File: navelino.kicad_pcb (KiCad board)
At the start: 2 copper layers, 45.6 x 37.3 mm, 73 parts, among them CON1 USB, IC1 ATMEGA328P-A, M1 CONN_1, M2 CONN_1, P1 CONN_02X03, P3 CONN_6, SW0 SW_PUSH, SW1 SMD-SWITCH-TACTILE-SPST-NO(4P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, SW2 SMD-SWITCH-TACTILE-SPST-NO(4P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, U1 XC6204B332MR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

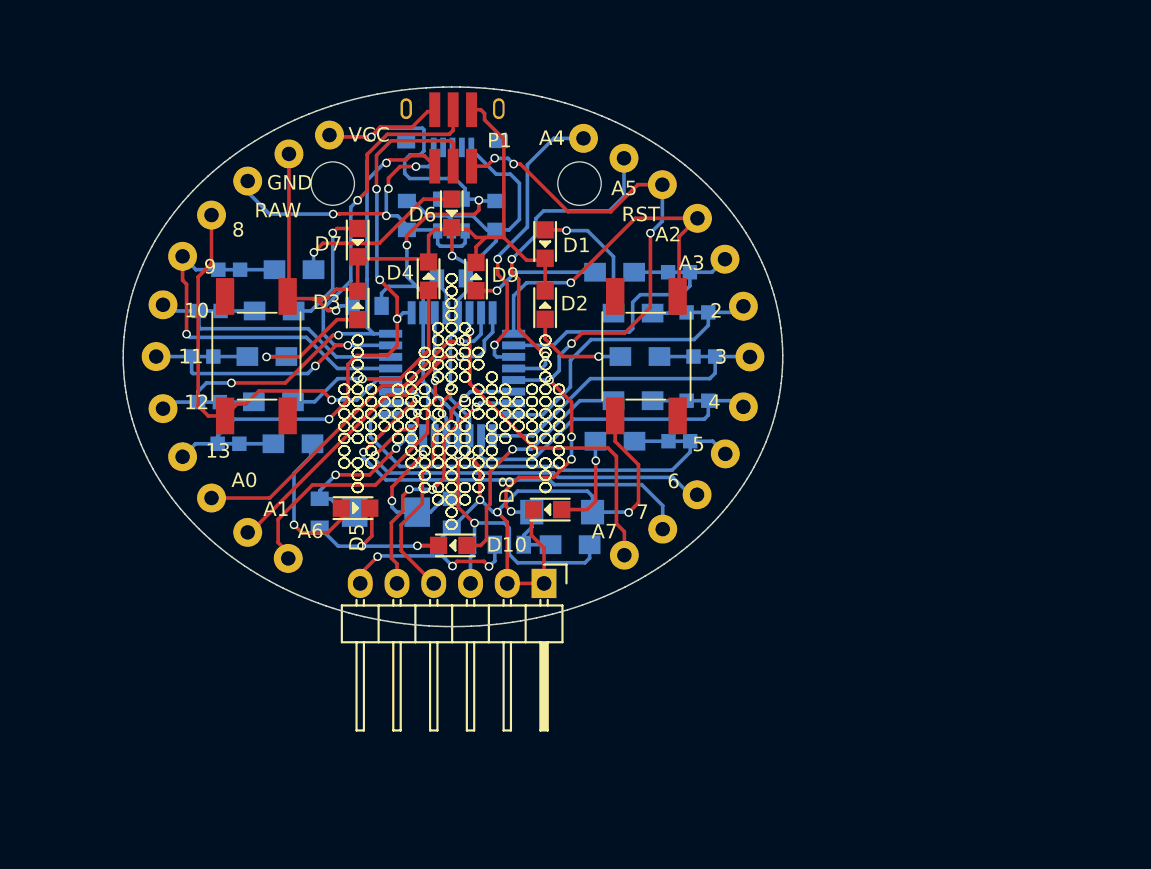
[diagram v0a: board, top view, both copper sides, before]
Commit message: Empezando rev3
- Permitir hojas intercambiables, conector SPI completo
- Usar charlieplexing para reducir el numero de GPIOS para los leds a 4
en vez de 10
- Eliminar el botón de reset, se usara una pulsación prolongada de los
dos botones de disparo para hacer un reset software
- Añadir soporte V-USB en el cuerpo
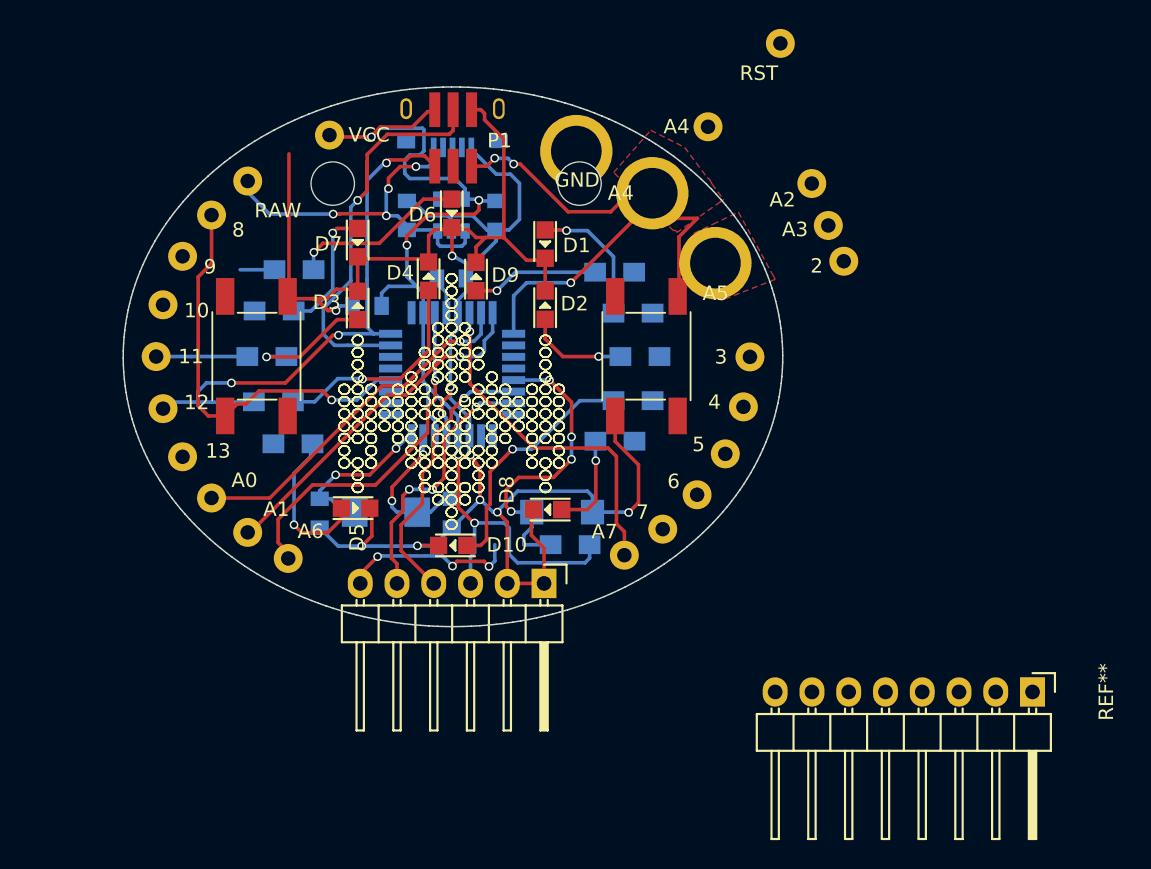
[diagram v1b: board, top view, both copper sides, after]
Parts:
- removed C4: 0.1uF, Capacitors_SMD:C_0805
- removed JP1, JP10, JP2, JP3, JP4, JP5, JP6, JP7, JP8, JP9: JUMPER, Wire_Connections_Bridges:PCB_JUMPER
- added A4: CONN_1, Wire_Pads:SolderWirePad_single_1mmDrill, F.Cu at (138.8, 117.9)
- added REF**: Pin_Header_Angled_1x08, Pin_Headers:Pin_Header_Angled_1x08, F.Cu at (165.1, 152.4)
- moved GND 19.9 mm to (133.6, 115.0)
- moved RST 12.7 mm to (147.7, 107.6)
- moved A5 9.61 mm to (143.2, 122.8)
- moved A4 8.64 mm to (142.7, 113.3)
- moved A2 8.26 mm to (149.8, 117.3)
- moved 2 7.60 mm to (152.1, 122.6)
- moved A3 7.51 mm to (151.0, 120.2)
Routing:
- net PB5/SCK: track 43.6 -> 0.00 mm, vias 4 -> 0
- net RESET: track 55.6 -> 22.4 mm, vias 8 -> 4
- net PD7: track 31.4 -> 0.00 mm, vias 2 -> 0
- net PD6: track 30.3 -> 0.00 mm, vias 2 -> 0
- net PD5: track 29.8 -> 0.00 mm
- net PB1: track 24.9 -> 0.00 mm, vias 1 -> 0
- net SCL: track 23.8 -> 0.00 mm, vias 2 -> 0
- net PD4: track 22.1 -> 0.00 mm
- net PD3: track 20.7 -> 0.00 mm
- net PD2: track 20.6 -> 0.00 mm
- net PB2: track 19.4 -> 0.00 mm
- net PC3: track 18.7 -> 0.00 mm
- net PB3/MOSI: track 45.4 -> 32.7 mm, vias 3 -> 1
- net PC2: track 23.6 -> 13.1 mm
- net SDA: track 20.6 -> 25.3 mm
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- added copper zone on F.Cu, net SCL
- added copper zone on F.Cu, net SDA

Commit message: Casi finalizado el nuevo esquema
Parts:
- removed M1, M2: CONN_1, Mounting_Holes:MountingHole_3mm
- removed SW0: SW_PUSH, SEEED:B3U-1000P
- moved 12 8.19 mm to (96.8, 132.6)
- moved 11 7.80 mm to (96.8, 128.9)
- moved 10 7.65 mm to (98.0, 122.7)
- moved 9 7.64 mm to (100.2, 117.8)
- moved 8 7.59 mm to (103.2, 113.9)
- moved VCC 6.45 mm to (113.0, 108.5)
- moved RAW 4.98 mm to (108.4, 112.8)
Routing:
- net PB4/MISO: track 36.3 -> 31.4 mm
- net Net-(JP4-Pad2): track 2.36 -> 7.22 mm
- net Net-(JP3-Pad2): track 2.35 -> 6.30 mm
- net PB3/MOSI: track 32.7 -> 28.7 mm
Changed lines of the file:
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@@
 (kicad_pcb (version 4) (host pcbnew 4.0.4-stable)
   (general
-    (links 87)
-    (no_connects 20)
-    (area 94.182046 58.551099 172.79981 163.275001)
+    (links 85)
+    (no_connects 24)
+    (area 102.222792 110.550044 147.892131 147.934279)
     (thickness 1.6)
     (drawings 28316)
     (tracks 499)
     (zones 0)
-    (modules 64)
-    (nets 61)
+    (modules 61)
+    (nets 59)
   )
   (page A4)
@@
     (34 B.Paste user hide)
     (35 F.Paste user hide)
-    (36 B.SilkS user hide)
-    (37 F.SilkS user hide)
+    (36 B.SilkS user)
+    (37 F.SilkS user)
     (38 B.Mask user)
     (39 F.Mask user)
@@
     (pad_to_mask_clearance 0)
     (aux_axis_origin 0 0)
-    (visible_elements FFFEFD7F)
+    (visible_elements FFFEFF7F)
     (pcbplotparams
       (layerselection 0x01030_80000001)
@@
   (net 57 "Net-(SW2-Pad2)")
   (net 58 "Net-(SW2-Pad4)")
-  (net 59 "Net-(M1-Pad1)")
-  (net 60 "Net-(M2-Pad1)")
   (net_class Default "This is the default net class."
     (clearance 0.2)
@@
     (add_net "Net-(JP8-Pad2)")
     (add_net "Net-(JP9-Pad2)")
-    (add_net "Net-(M1-Pad1)")
-    (add_net "Net-(M2-Pad1)")
     (add_net "Net-(SW1-Pad2)")
     (add_net "Net-(SW1-Pad4)")
@@
       (net 17 SDA))
   )
-  (module Mounting_Holes:MountingHole_3mm (layer F.Cu)
-    (at 116.75 117.275)
-    (descr "Mounting hole, Befestigungsbohrung, 3mm, No Annular, Kein Restring,")
-    (tags "Mounting hole, Befestigungsbohrung, 3mm, No Annular, Kein Restring,")
-    (fp_text reference M1 (at 0 -4.0005) (layer F.SilkS) hide
-      (effects (font (size 1 1) (thickness 0.15)))
-    )
-    (fp_text value CONN_1 (at 1.00076 5.00126) (layer F.Fab)
-      (effects (font (size 1 1) (thickness 0.15)))
-    )
-    (fp_circle (center 0 0) (end 3 0) (layer Cmts.User) (width 0.381))
-    (pad 1 thru_hole circle (at 0 0) (size 3 3) (drill 3) (layers)
-      (net 59 "Net-(M1-Pad1)"))
-  )
   (module SMD-CRYSTAL-8MHZ-20PF-20PPM_2P-5.0X3.2MM_:X2-SMD-5.0X3.2X1.3MM (layer B.Cu)
     (at 120.425 139.975 180)
@@
   )
   (module Wire_Pads:SolderWirePad_single_1mmDrill (layer F.Cu)
-    (at 108.375 119.45)
+    (at 103.24 113.86)
     (fp_text reference 8 (at 1.85 1.025) (layer F.SilkS)
       (effects (font (size 1 1) (thickness 0.15)))
@@
   )
   (module Wire_Pads:SolderWirePad_single_1mmDrill (layer F.Cu)
-    (at 106.375 122.3)
+    (at 100.22 117.77)
     (fp_text reference 9 (at 1.9 0.725) (layer F.SilkS)
       (effects (font (size 1 1) (thickness 0.15)))
@@
   )
   (module Wire_Pads:SolderWirePad_single_1mmDrill (layer F.Cu)
-    (at 105.025 125.65)
+    (at 97.96 122.71)
     (fp_text reference 10 (at 2.325 0.4) (layer F.SilkS)
       (effects (font (size 1 1) (thickness 0.15)))
@@
   )
   (module Wire_Pads:SolderWirePad_single_1mmDrill (layer F.Cu)
-    (at 104.55 129.225)
+    (at 96.76 128.86)
     (fp_text reference 11 (at 2.4 0) (layer F.SilkS)
       (effects (font (size 1 1) (thickness 0.15)))
@@
   )
   (module Wire_Pads:SolderWirePad_single_1mmDrill (layer F.Cu)
-    (at 105.025 132.825)
+    (at 96.84 132.58)
     (fp_text reference 12 (at 2.325 -0.425) (layer F.SilkS)
       (effects (font (size 1 1) (thickness 0.15)))
@@
   )
   (module Wire_Pads:SolderWirePad_single_1mmDrill (layer F.Cu)
-    (at 116.525 113.925)
+    (at 112.96 108.55)
     (fp_text reference VCC (at 2.735 -0.015) (layer F.SilkS)
       (effects (font (size 1 1) (thickness 0.15)))
@@
   )
   (module Wire_Pads:SolderWirePad_single_1mmDrill (layer F.Cu)
-    (at 110.875 117.1)
+    (at 108.41 112.77)
     (fp_text reference RAW (at 2.085 2.04) (layer F.SilkS)
       (effects (font (size 1 1) (thickness 0.15)))
@@
     )
   )
-  (module SEEED:B3U-1000P (layer B.Cu)
-    (at 132.6 139.975)
-    (fp_text reference SW0 (at 0 -2.286) (layer B.SilkS) hide
-      (effects (font (size 1 1) (thickness 0.15)) (justify mirror))
-    )
-    (fp_text value SW_PUSH (at 0 2.286) (layer B.Fab)
-      (effects (font (size 1 1) (thickness 0.15)) (justify mirror))
-    )
-    (fp_circle (center 0 0) (end 0.508 0.508) (layer B.SilkS) (width 0.15))
-    (fp_line (start 1.5 1.25) (end 1.5 -1.25) (layer B.SilkS) (width 0.15))
-    (fp_line (start 1.5 -1.25) (end -1.5 -1.25) (layer B.SilkS) (width 0.15))
-    (fp_line (start -1.5 1.25) (end 1.5 1.25) (layer B.SilkS) (width 0.15))
-    (fp_line (start -1.5 1.25) (end -1.5 -1.25) (layer B.SilkS) (width 0.15))
-    (pad 1 smd rect (at -2.1 0) (size 1.6 1.7) (layers B.Cu B.Paste B.Mask)
-      (net 19 RESET))
-    (pad 2 smd rect (at 2.1 0) (size 1.6 1.7) (layers B.Cu B.Paste B.Mask)
-      (net 1 GND))
-  )
   (module Resistors_SMD:R_0805_HandSoldering (layer B.Cu)
     (at 133.15 142.225)
@@
     )
   )
-  (module Mounting_Holes:MountingHole_3mm (layer F.Cu)
-    (at 133.8 117.275)
-    (descr "Mounting hole, Befestigungsbohrung, 3mm, No Annular, Kein Restring,")
-    (tags "Mounting hole, Befestigungsbohrung, 3mm, No Annular, Kein Restring,")
-    (fp_text reference M2 (at 0 -4.0005) (layer F.SilkS) hide
-      (effects (font (size 1 1) (thickness 0.15)))
-    )
-    (fp_text value CONN_1 (at 1.00076 5.00126) (layer F.Fab)
-      (effects (font (size 1 1) (thickness 0.15)))
-    )
-    (fp_circle (center 0 0) (end 3 0) (layer Cmts.User) (width 0.381))
-    (pad 1 thru_hole circle (at 0 0) (size 3 3) (drill 3) (layers)
-      (net 60 "Net-(M2-Pad1)"))
-  )
   (module navelino:ISPSMD (layer F.Cu)
     (at 125.07 114.12)
@@
   (segment (start 124.800002 113.869998) (end 125.07 113.6) (width 0.25) (layer F.Cu) (net 28))
   (segment (start 125.07 113.6) (end 125.07 112.17) (width 0.25) (layer F.Cu) (net 28))
-  (segment (start 107 129.225) (end 108.5 129.225) (width 0.25) (layer B.Cu) (net 28))
   (segment (start 118 124) (end 118 118.9) (width 0.25) (layer B.Cu) (net 28))
   (via (at 118.47 118.43) (size 0.6) (drill 0.4) (layers F.Cu B.Cu) (net 28))
@@
   (segment (start 118 118.9) (end 118.47 118.43) (width 0.25) (layer B.Cu) (net 28))
   (segment (start 117.8 128.45) (end 120.75 128.45) (width 0.25) (layer B.Cu) (net 28) (status 20))
-  (segment (start 107 129.225) (end 104.55 129.225) (width 0.25) (layer B.Cu) (net 28) (status 30))
   (segment (start 119.12 117.81) (end 119.12 117.05) (width 0.25) (layer B.Cu) (net 29))
   (segment (start 123.08 115.35) (end 123.8 116.07) (width 0.25) (layer F.Cu) (net 29))
@@
   (segment (start 120.32 115.85) (end 120.46 115.85) (width 0.25) (layer B.Cu) (net 29))
   (segment (start 119.12 117.05) (end 120.32 115.85) (width 0.25) (layer B.Cu) (net 29))
-  (segment (start 107.45 132.375) (end 108.95 132.375) (width 0.25) (layer B.Cu) (net 29))
   (segment (start 119.12 123.895) (end 119.125 123.9) (width 0.25) (layer B.Cu) (net 29))
   (segment (start 119.12 117.81) (end 119.12 123.895) (width 0.25) (layer B.Cu) (net 29))
@@
   (segment (start 117.25 127.65) (end 117.15 127.75) (width 0.25) (layer B.Cu) (net 29))
   (segment (start 120.75 127.65) (end 119.575 127.65) (width 0.25) (layer B.Cu) (net 29) (status 10))
-  (segment (start 107.45 131.625) (end 107.45 132.375) (width 0.25) (layer B.Cu) (net 29) (status 20))
   (via (at 117.15 127.75) (size 0.6) (drill 0.4) (layers F.Cu B.Cu) (net 29))
   (segment (start 117.15 127.75) (end 117.144301 127.755699) (width 0.25) (layer F.Cu) (net 29))
@@
   (segment (start 109.75 131.05) (end 108.025 131.05) (width 0.25) (layer B.Cu) (net 29))
   (segment (start 108.025 131.05) (end 107.45 131.625) (width 0.25) (layer B.Cu) (net 29))
-  (segment (start 105.475 132.375) (end 105.025 132.825) (width 0.25) (layer B.Cu) (net 29) (status 30))
-  (segment (start 107.45 132.375) (end 105.475 132.375) (width 0.25) (layer B.Cu) (net 29) (status 30))
   (segment (start 110.875 117.1) (end 110.875 117.865) (width 0.25) (layer B.Cu) (net 32) (status 30))
   (segment (start 110.875 117.865) (end 112.39 119.38) (width 0.25) (layer B.Cu) (net 32) (status 10))
@@
   (segment (start 130.475 135.625) (end 129.175 135.625) (width 0.25) (layer B.Cu) (net 40))
   (segment (start 133.825 132.275) (end 130.475 135.625) (width 0.25) (layer B.Cu) (net 40))
+  (segment (start 107 129.225) (end 108.5 129.225) (width 0.25) (layer B.Cu) (net 43))
+  (segment (start 107 129.225) (end 104.55 129.225) (width 0.25) (layer B.Cu) (net 43) (status 30))
   (segment (start 108.5 129.225) (end 110.85 129.225) (width 0.25) (layer B.Cu) (net 43) (status 30))
+  (segment (start 107.45 132.375) (end 108.95 132.375) (width 0.25) (layer B.Cu) (net 44))
+  (segment (start 107.45 131.625) (end 107.45 132.375) (width 0.25) (layer B.Cu) (net 44) (status 20))
+  (segment (start 105.475 132.375) (end 105.025 132.825) (width 0.25) (layer B.Cu) (net 44) (status 30))
+  (segment (start 107.45 132.375) (end 105.475 132.375) (width 0.25) (layer B.Cu) (net 44) (status 30))
   (segment (start 111.275 132.375) (end 111.3 132.35) (width 0.25) (layer B.Cu) (net 44) (status 30))
   (segment (start 108.95 132.375) (end 111.275 132.375) (width 0.25) (layer B.Cu) (net 44) (status 30))
